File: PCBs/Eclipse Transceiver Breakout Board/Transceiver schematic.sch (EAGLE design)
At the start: 3 parts, among them J1 2X6 FEMALE, U1 RFM95W-868S2

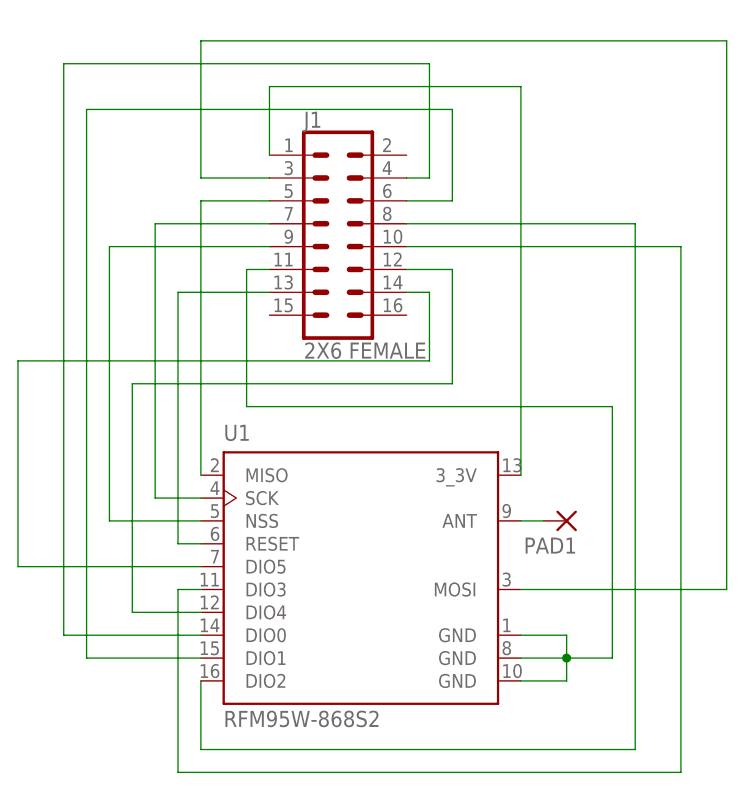
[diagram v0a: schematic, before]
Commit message: Final Update
This is the design for the board that was milled and used for the RTR testing.
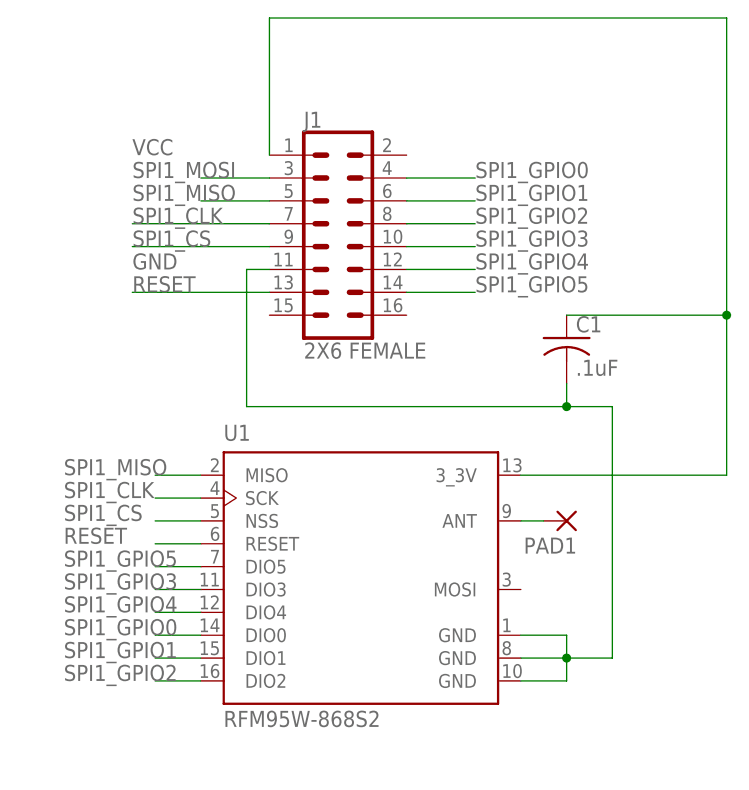
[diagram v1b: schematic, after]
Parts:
- added C1: .1uF, RTR:C-ALL_PACKAGESC1206
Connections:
- net N$10 renamed SPI1_GPIO3
- net N$11 renamed SPI1_GPIO4
- net N$13 renamed RESET
- net N$14 renamed SPI1_GPIO5
- net N$3 renamed SPI1_MISO
- net N$4 renamed SPI1_CLK
- net N$6 renamed SPI1_GPIO0
- net N$7 renamed SPI1_CS
- net N$8 renamed SPI1_GPIO1
- net N$9 renamed SPI1_GPIO2
- removed net N$1: J1.11, U1.GND, U1.GND@1, U1.GND@2
- removed net N$2: J1.3, U1.MOSI
- removed net N$5: J1.1, U1.3_3V
- new net GND: C1.2, J1.11, U1.GND, U1.GND@1, U1.GND@2
- new net SPI1_MOSI: J1.3
- new net VCC: C1.1, J1.1, U1.3_3V
